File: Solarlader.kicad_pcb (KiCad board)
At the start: 2 copper layers, 32.8 x 29 mm, 40 parts, among them J3 UKDBBTAAA, Q1 HJ8205, Q2 AO3400A, U1 LGS5600, U2 DW01A, U3 74AHC1G14GV,125

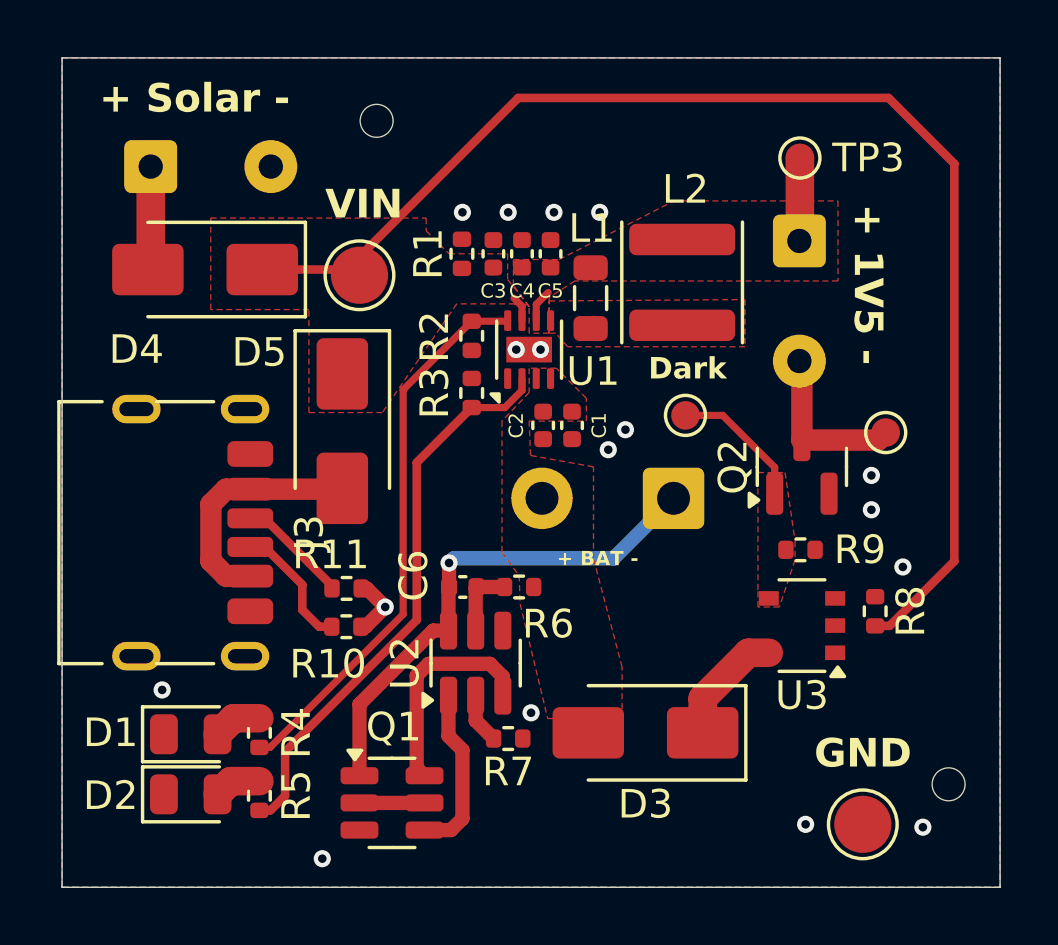
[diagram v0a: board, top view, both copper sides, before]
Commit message: Stand mit 1.5V
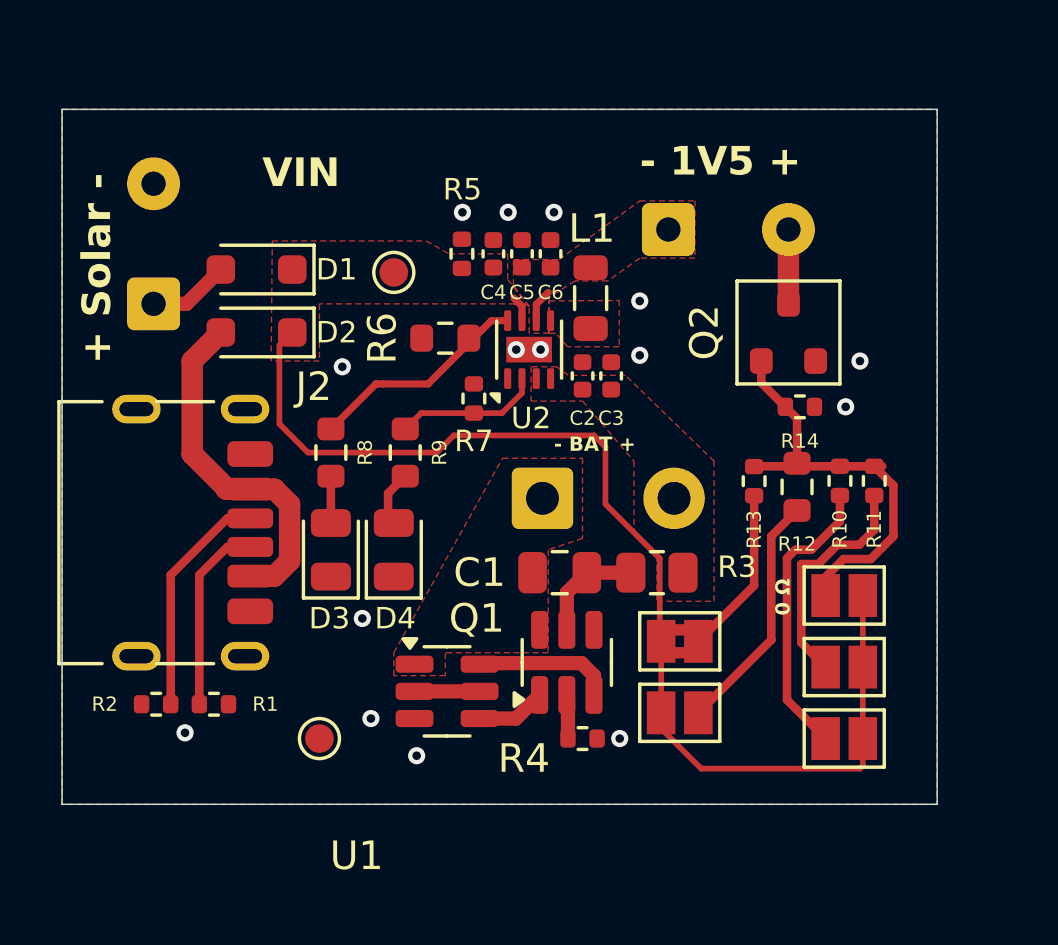
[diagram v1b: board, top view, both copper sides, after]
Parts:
- removed the D3 at (156.4, 95.4)
- removed L2: 2.2u, Inductor_SMD:L_APV_ANR4010
- removed the R8 at (164.4, 91.2)
- removed the R9 at (161.8, 89.0)
- removed REF** (x2): ToolingHole_1.152mm, MountingHole:ToolingHole_1.152mm
- removed TP3: +1V5, TestPoint:TestPoint_Pad_D1.0mm
- removed TP5: Switch+, TestPoint:TestPoint_Pad_D1.0mm
- removed TP6: Dark, TestPoint:TestPoint_Pad_D1.0mm
- removed U3: 74AHC1G14GV,125, Package_SO:TSOP-5_1.65x3.05mm_P0.95mm
- added JP1: SolderJumper_2_Open, Jumper:SolderJumper-2_P1.3mm_Open_Pad1.0x1.5mm, F.Cu at (163.3, 90.6)
- added JP2: SolderJumper_2_Open, Jumper:SolderJumper-2_P1.3mm_Open_Pad1.0x1.5mm, F.Cu at (163.3, 95.6)
- added JP3: SolderJumper_2_Open, Jumper:SolderJumper-2_P1.3mm_Open_Pad1.0x1.5mm, F.Cu at (163.3, 93.1)
- added JP4: SolderJumper_2_Open, Jumper:SolderJumper-2_P1.3mm_Open_Pad1.0x1.5mm, F.Cu at (157.6, 94.7)
- added JP5: SolderJumper_2_Bridged, Jumper:SolderJumper-2_P1.3mm_Bridged2Bar_Pad1.0x1.5mm, F.Cu at (157.6, 92.2)
- added R10: 2.2k, Resistor_SMD:R_0402_1005Metric, F.Cu at (163.2, 86.6)
- added R11: 5.1k, Resistor_SMD:R_0402_1005Metric, F.Cu at (164.4, 86.6)
- added R12: 8.2k, Resistor_SMD:R_0603_1608Metric, F.Cu at (161.7, 86.8)
- added R13: 10k, Resistor_SMD:R_0402_1005Metric, F.Cu at (160.2, 86.6)
- added R14: 100k, Resistor_SMD:R_0402_1005Metric, F.Cu at (161.8, 84.0)
- C1: renamed from C6; footprint Capacitor_SMD:C_0402_1005Metric -> Capacitor_SMD:C_0805_2012Metric
- D1: renamed from D4; value MDD SS14 -> 1N5819WS; footprint Diode_SMD:D_SMA -> Diode_SMD:D_SOD-323_HandSoldering
- D2: renamed from D5; value MDD SS14 -> 1N5819WS; footprint Diode_SMD:D_SMA -> Diode_SMD:D_SOD-323_HandSoldering
- Q2: footprint Package_TO_SOT_SMD:SOT-23 -> PCM_Package_TO_SOT_SMD_AKL:SOT-23
- R3: renamed from R6; footprint Resistor_SMD:R_0402_1005Metric -> Resistor_SMD:R_0805_2012Metric
- R6: renamed from R2; value 27k -> 30k; footprint Resistor_SMD:R_0402_1005Metric -> Resistor_SMD:R_0603_1608Metric
- R8: renamed from R4; value 150 -> 1.5k; footprint Resistor_SMD:R_0402_1005Metric -> Resistor_SMD:R_0603_1608Metric
- R9: renamed from R5; value 75 -> 1k; footprint Resistor_SMD:R_0402_1005Metric -> Resistor_SMD:R_0603_1608Metric
- TP1: renamed from TP2; footprint TestPoint:TestPoint_Pad_D2.0mm -> TestPoint:TestPoint_Pad_D1.0mm
- TP2: renamed from TP7; value Switch- -> GND; footprint TestPoint:TestPoint_Pad_D2.0mm -> TestPoint:TestPoint_Pad_D1.0mm
- moved TP2 19.2 mm to (145.0, 95.6)
- moved R9 13.0 mm to (148.0, 85.6), turned to -90 degrees
- moved D4 11.1 mm to (147.6, 89.0), turned to 90 degrees
- moved R8 10.1 mm to (145.4, 85.6), turned to -90 degrees
- moved D3 8.10 mm to (145.4, 89.0), turned to 90 degrees
- moved R2 7.79 mm to (139.3, 94.4), turned to 180 degrees
- moved R1 5.36 mm to (141.3, 94.4)
- moved R3 4.84 mm to (156.8, 89.8)
- moved J1 4.80 mm to (139.2, 80.4), turned to 90 degrees
- moved Q2 4.72 mm to (161.4, 81.4)
- moved J3 4.60 mm to (157.2, 77.8), turned to 0 degrees
- moved BT1 4.58 mm to (152.8, 87.2), turned to 0 degrees
- moved D2 4.57 mm to (142.8, 81.4), turned to 180 degrees
- moved Q1 4.35 mm to (149.5, 94.0)
- moved C1 3.42 mm to (153.4, 89.8)
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- renumbered C1 to C2, C2 to C3, C3 to C4, C4 to C5, C5 to C6, D1 to D3, D2 to D4, J2 to J1, J3 to J2, J1 to J3, R10 to R1, R11 to R2, R7 to R4, R1 to R5, R3 to R7, U2 to U1, U1 to U2
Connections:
- net /Switch+ renamed /Load+
- Q2 pad 1: /Dark -> Net-(JP1-A)
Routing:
- net /BAT-: track 18.5 -> 0.00 mm, vias 1 -> 0
- net Net-(JP1-A): track 0.00 -> 15.1 mm
- net Net-(U2-VSET/LED1): track 19.8 -> 5.11 mm
- net Net-(U2-ISET/LED2): track 19.5 -> 8.00 mm
- net Net-(JP2-A): track 0.00 -> 10.2 mm
- net Net-(JP4-A): track 0.00 -> 8.50 mm
- net Net-(JP3-A): track 0.00 -> 8.20 mm
- net Net-(JP5-A): track 0.00 -> 5.90 mm
- net Vin: track 46.2 -> 40.8 mm
- net /VBUS: track 8.40 -> 13.2 mm
- net /Dark: track 4.79 -> 0.00 mm
- net Net-(J2-CC1): track 4.16 -> 8.72 mm
- net Net-(D3-K): track 4.17 -> 0.00 mm
- net Net-(Q1-G1): track 5.99 -> 2.44 mm
- net /Load+: track 5.98 -> 2.60 mm
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- added copper zone on F.Cu, net /BAT-
- removed copper zone on F.Cu, net /Dark
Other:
- board size 32.8 x 29 mm -> 30.6 x 24.3 mm
- board text added: "- 1V5 +"
- board text added: "- BAT +"
- board text added: "0 Ω"
- board text removed: "+ 1V5 -"
- board text removed: "+ BAT -"
- board text removed: "Dark"
- board text removed: "GND"

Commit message: V2
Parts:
- removed JP1, JP2, JP3, JP4: SolderJumper_2_Open, Jumper:SolderJumper-2_P1.3mm_Open_Pad1.0x1.5mm
- removed JP5: SolderJumper_2_Bridged, Jumper:SolderJumper-2_P1.3mm_Bridged2Bar_Pad1.0x1.5mm
- removed Q2: AO3400A, PCM_Package_TO_SOT_SMD_AKL:SOT-23
- removed TP2: GND, TestPoint:TestPoint_Pad_D1.0mm
- added C10: 100u, Capacitor_Tantalum_SMD:CP_EIA-3528-21_Kemet-B, F.Cu at (178.5, 119.0)
- added C7: 10u, Capacitor_SMD:C_0603_1608Metric, F.Cu at (149.3, 107.0)
- added C8: 10u, Capacitor_SMD:C_0402_1005Metric, F.Cu at (152.9, 122.9)
- added C9: 20u, Capacitor_SMD:C_1206_3216Metric, F.Cu at (181.0, 129.5)
- added D5: KT-0805G, LED_SMD:LED_0805_2012Metric, F.Cu at (170.7, 105.2)
- added L2: 2.2u, Inductor_SMD:L_APV_ANR4020, F.Cu at (158.2, 124.8)
- added R15: 100k, Resistor_SMD:R_0402_1005Metric, F.Cu at (173.7, 124.8)
- added R16: 100, Resistor_SMD:R_0402_1005Metric, F.Cu at (173.7, 126.8)
- added R17: 100k, Resistor_SMD:R_0402_1005Metric, F.Cu at (173.7, 128.8)
- added R18: 0, Resistor_SMD:R_0603_1608Metric, F.Cu at (153.3, 109.5)
- added R19: 0, Resistor_SMD:R_0603_1608Metric, F.Cu at (153.3, 112.0)
- added U3: DW01A, Package_TO_SOT_SMD:SOT-23-6, F.Cu at (171.9, 113.8)
- added U4: TPS61022, Package_DFN_QFN:Texas_RWU0007A_VQFN-7_2x2mm_P0.5mm, F.Cu at (149.5, 125.2)
- BT1: footprint Connector_Wire:SolderWire-0.5sqmm_1x02_P4.6mm_D0.9mm_OD2.1mm -> Connector_JST:JST_PH_S2B-PH-K_1x02_P2.00mm_Horizontal
- C1: value 100n -> 100u; footprint Capacitor_SMD:C_0805_2012Metric -> Capacitor_Tantalum_SMD:CP_EIA-3528-21_Kemet-B
- C2, C4: footprint Capacitor_SMD:C_0402_1005Metric -> Capacitor_SMD:C_0603_1608Metric
- C3: value 10u -> 20u; footprint Capacitor_SMD:C_0402_1005Metric -> Capacitor_SMD:C_1206_3216Metric
- C5: value 10u -> 1u
- C6: value 10u -> 100n; footprint Capacitor_SMD:C_0402_1005Metric -> Capacitor_SMD:C_0805_2012Metric
- D1, D2: value 1N5819WS -> DSL34; footprint Diode_SMD:D_SOD-323_HandSoldering -> Diode_SMD:D_SOD-123F
- D3: value KT-0805Y -> DSL34; footprint LED_SMD:LED_0805_2012Metric -> Diode_SMD:D_SOD-123F
- D4: value KT-0805G -> KT-0805Y
- J1, J3: footprint Connector_Wire:SolderWire-0.25sqmm_1x02_P4.2mm_D0.65mm_OD1.7mm -> Connector_Wire:SolderWire-0.1sqmm_1x02_P3.6mm_D0.4mm_OD1mm
- L1: footprint Inductor_SMD:L_0805_2012Metric -> Inductor_SMD:L_APV_ANR4020
- R10: value 2.2k -> 1.6k; footprint Resistor_SMD:R_0402_1005Metric -> Resistor_SMD:R_0603_1608Metric
- R11: value 5.1k -> 1k
- R12: value 8.2k -> 51k; footprint Resistor_SMD:R_0603_1608Metric -> Resistor_SMD:R_0402_1005Metric
- R13: value 10k -> 680k; footprint Resistor_SMD:R_0402_1005Metric -> Resistor_SMD:R_0603_1608Metric
- R14: value 100k -> 2k
- R3: value 100 -> 51k; footprint Resistor_SMD:R_0805_2012Metric -> Resistor_SMD:R_0402_1005Metric
- R4: value 1k -> 680k; footprint Resistor_SMD:R_0402_1005Metric -> Resistor_SMD:R_0603_1608Metric
- R5: value 1k -> 2k
- R6: value 30k -> 100k; footprint Resistor_SMD:R_0603_1608Metric -> Resistor_SMD:R_0402_1005Metric
- R7: value 10k -> 1k; footprint Resistor_SMD:R_0402_1005Metric -> Resistor_SMD:R_0603_1608Metric
- R8: value 1.5k -> 1k
- R9: value 1k -> 100; footprint Resistor_SMD:R_0603_1608Metric -> Resistor_SMD:R_0805_2012Metric
- TP1: value VIn -> GND
- U1: value DW01A -> TPS61022; footprint Package_TO_SOT_SMD:SOT-23-6 -> Package_DFN_QFN:Texas_RWU0007A_VQFN-7_2x2mm_P0.5mm
- U2: value LGS5600 -> TP4056; footprint Package_DFN_QFN:DFN-8-1EP_2x2mm_P0.5mm_EP0.9x1.6mm -> Package_SO:SOP-8-1EP_4.57x4.57mm_P1.27mm_EP4.57x4.45mm
- moved J2 75.0 mm to (210.1, 113.3), turned to 90 degrees
- moved R2 72.3 mm to (206.7, 120.6), turned to -90 degrees
- moved R1 71.3 mm to (207.6, 120.6), turned to -90 degrees
- moved J1 68.9 mm to (201.8, 109.2), turned to 180 degrees
- moved D2 67.9 mm to (203.2, 112.2), turned to 0 degrees
- moved U2 65.3 mm to (198.6, 128.1), turned to 0 degrees
- moved D1 65.0 mm to (198.8, 112.2)
- moved C1 56.5 mm to (203.5, 116.0), turned to -90 degrees
- moved C2 56.2 mm to (198.8, 117.2), turned to -90 degrees
- moved C3 52.4 mm to (193.5, 118.7)
- moved R5 51.3 mm to (167.9, 126.8), turned to 0 degrees
- moved R6 50.7 mm to (167.9, 128.8), turned to 0 degrees
- moved C6 50.4 mm to (163.2, 128.0), turned to 0 degrees
- moved U1 49.9 mm to (196.5, 118.5), turned to 0 degrees
- moved TP1 46.4 mm to (153.0, 125.4)
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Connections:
- BT1 pad 1: /BAT- -> +BATT
- BT1 pad 2: /BAT+ -> /BAT-
- C1 pad 1: Net-(U1-VCC) -> /VIN
- C1 pad 2: /BAT- -> GND
- C2 pad 1: /BAT+ -> /VIN
- C3 pad 1: /BAT+ -> +5V
- C4 pad 1: Vin -> +5V
- C5 pad 1: +1V5 -> +5V
- C6 pad 1: +1V5 -> Net-(U3-VCC)
- C6 pad 2: GND -> /BAT-
- D1 pad 1: Vin -> /VIN
- D2 pad 1: Vin -> /VIN
- D3 pad 1: GND -> +5V
- D3 pad 2: Net-(D3-A) -> /VIN
- D4 pad 1: GND -> Net-(D4-K)
- D4 pad 2: Net-(D4-A) -> +5V
- J3 pad 1: +1V5 -> /VIN
- L1 pad 1: Net-(U2-LX) -> /VIN
- L1 pad 2: +1V5 -> Net-(U1-SW)
- R10 pad 1: Net-(JP2-A) -> Net-(U2-PROG)
- R10 pad 2: Net-(JP1-A) -> GND
- R11 pad 1: Net-(JP3-A) -> GND
- R11 pad 2: Net-(JP1-A) -> Net-(U3-CS)
- R12 pad 1: Net-(JP4-A) -> +4V5
- R12 pad 2: Net-(JP1-A) -> Net-(R12-Pad2)
- R13 pad 1: Net-(JP5-A) -> Net-(R12-Pad2)
- R13 pad 2: Net-(JP1-A) -> Net-(R13-Pad2)
- R14 pad 1: Net-(JP1-A) -> Net-(R13-Pad2)
- R14 pad 2: GND -> Net-(U4-FB)
- R3 pad 1: /BAT+ -> +5V
- R3 pad 2: Net-(U1-VCC) -> Net-(R3-Pad2)
- R4 pad 1: GND -> Net-(R3-Pad2)
- R4 pad 2: Net-(U1-CS) -> Net-(R4-Pad2)
- R5 pad 1: Vin -> Net-(R4-Pad2)
- R5 pad 2: GND -> Net-(U1-FB)
- R6 pad 1: Net-(U2-ISET/LED2) -> Net-(U1-FB)
- R7 pad 1: GND -> Net-(D4-K)
- R7 pad 2: Net-(U2-VSET/LED1) -> Net-(U2-STDBY)
- R8 pad 1: Net-(U2-ISET/LED2) -> Net-(D5-K)
- R8 pad 2: Net-(D3-A) -> Net-(U2-~{CHRG})
- R9 pad 1: Net-(U2-VSET/LED1) -> +BATT
- R9 pad 2: Net-(D4-A) -> Net-(U3-VCC)
- TP1 pad 1: Vin -> GND
- U1 pad 1: Net-(Q1-G1) -> GND
- U1 pad 2: Net-(U1-CS) -> Net-(U1-SW)
- U1 pad 3: Net-(Q1-G2) -> +5V
- U1 pad 4: unconnected-(U1-TD-Pad4) -> Net-(U1-FB)
- U1 pad 5: Net-(U1-VCC) -> /VIN
- U1 pad 6: /BAT- -> GND
- U2 pad 1: GND -> Net-(U2-~{CHRG})
- U2 pad 2: Net-(U2-VSET/LED1) -> GND
- U2 pad 3: /BAT+ -> +BATT
- U2 pad 4: /BAT+ -> +5V
- U2 pad 5: Net-(U2-LX) -> Net-(U2-STDBY)
- U2 pad 6: +1V5 -> Net-(U2-PROG)
- U2 pad 7: Vin -> (no net)
- U2 pad 8: Net-(U2-ISET/LED2) -> (no net)
- U2 pad 9: GND -> (no net)
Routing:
- net Vin: track 40.8 -> 0.00 mm
- net Net-(JP1-A): track 15.1 -> 0.00 mm
- net /VBUS: track 13.2 -> 0.00 mm
- net Net-(JP2-A): track 10.2 -> 0.00 mm
- net Net-(JP4-A): track 8.50 -> 0.00 mm
- net Net-(JP3-A): track 8.20 -> 0.00 mm
- net Net-(U2-ISET/LED2): track 8.00 -> 0.00 mm
- net Net-(JP5-A): track 5.90 -> 0.00 mm
- net Net-(U2-VSET/LED1): track 5.11 -> 0.00 mm
- net Net-(Q1-G2): track 4.87 -> 0.00 mm
- net GND: track 0.23 -> 4.99 mm, vias 15 -> 0
- net Net-(U1-VCC): track 3.83 -> 0.00 mm
- net /Solar+: track 3.45 -> 0.00 mm
- net Net-(J2-CC2): track 7.31 -> 10.4 mm
- net /Load+: track 2.60 -> 0.00 mm
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- added copper zone on In1.Cu, net GND
- added copper zone on In2.Cu, net GND
- removed copper zone on F.Cu, net +1V5
- removed copper zone on F.Cu, net /BAT+
- removed copper zone on F.Cu, net /BAT-
- removed copper zone on F.Cu, net GND
- removed copper zone on F.Cu, net Net-(U2-LX)
- removed copper zone on F.Cu, net Vin
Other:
- board size 30.6 x 24.3 mm -> 29 x 31.8 mm
- copper layers 2 -> 4
- rule pad_to_mask_clearance: 0 -> 0.038
- board text added: "- IN +"
- board text added: "USB 5V"
- board text removed: "+ Solar -"
- board text removed: "- 1V5 +"
- board text removed: "- BAT +"
- board text removed: "0 Ω"
- board text removed: "VIN"

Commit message: Saved between
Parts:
- removed C7: 10u, Capacitor_SMD:C_0603_1608Metric
- removed C8: 10u, Capacitor_SMD:C_0402_1005Metric
- removed C9: 20u, Capacitor_SMD:C_1206_3216Metric
- removed D5: KT-0805G, LED_SMD:LED_0805_2012Metric
- removed J3: ~, Connector_Wire:SolderWire-0.1sqmm_1x02_P3.6mm_D0.4mm_OD1mm
- removed L1, L2: 2.2u, Inductor_SMD:L_APV_ANR4020
- removed R10: 1.6k, Resistor_SMD:R_0603_1608Metric
- removed R12: 51k, Resistor_SMD:R_0402_1005Metric
- removed R13: 680k, Resistor_SMD:R_0603_1608Metric
- removed R14: 2k, Resistor_SMD:R_0402_1005Metric
- removed R15, R17: 100k, Resistor_SMD:R_0402_1005Metric
- removed R16: 100, Resistor_SMD:R_0402_1005Metric
- removed R18, R19: 0, Resistor_SMD:R_0603_1608Metric
- removed R8: 1k, Resistor_SMD:R_0603_1608Metric
- removed TP1: GND, TestPoint:TestPoint_Pad_D1.0mm
- removed U2: TP4056, Package_SO:SOP-8-1EP_4.57x4.57mm_P1.27mm_EP4.57x4.45mm
- removed U4: TPS61022, Package_DFN_QFN:Texas_RWU0007A_VQFN-7_2x2mm_P0.5mm
- added H1: MountingHole, MountingHole:MountingHole_2.2mm_M2_DIN965, F.Cu at (188.0, 108.4)
- added H2: MountingHole, MountingHole:MountingHole_2.2mm_M2_DIN965, F.Cu at (211.5, 127.1)
- C2: value 10u -> 2.2u 25V; footprint Capacitor_SMD:C_0603_1608Metric -> Capacitor_SMD:C_0805_2012Metric
- C3: value 20u -> 0.1u 25V; footprint Capacitor_SMD:C_1206_3216Metric -> Capacitor_SMD:C_0402_1005Metric
- C4: value 10u -> 1u 35V
- C5: value 1u -> 10p 10V
- D3: value DSL34 -> KT-0603W; footprint Diode_SMD:D_SOD-123F -> LED_SMD:LED_0603_1608Metric
- D4: value KT-0805Y -> KT-0603Y2; footprint LED_SMD:LED_0805_2012Metric -> LED_SMD:LED_0603_1608Metric
- R3: value 51k -> 18k
- R4: value 680k -> 620
- R5: value 2k -> 10k
- R6: value 100k -> 510
- R7: value 1k -> 300; footprint Resistor_SMD:R_0603_1608Metric -> Resistor_SMD:R_0402_1005Metric
- U1: value TPS61022 -> BQ25185; footprint Package_DFN_QFN:Texas_RWU0007A_VQFN-7_2x2mm_P0.5mm -> Snapeda:WSON10_DLH_TEX-L
- U3: value DW01A -> DW01A - C686633
- moved R7 56.5 mm to (205.2, 120.1), turned to 90 degrees
- moved R4 55.4 mm to (204.1, 117.9)
- moved C4 55.2 mm to (201.6, 122.1)
- moved C5 46.0 mm to (198.9, 120.1), turned to 90 degrees
- moved D3 43.6 mm to (207.2, 120.6), turned to 180 degrees
- moved R9 42.0 mm to (199.1, 123.0), turned to -90 degrees
- moved D4 41.8 mm to (207.2, 122.2), turned to 180 degrees
- moved Q1 38.3 mm to (206.3, 125.9), turned to 90 degrees
- moved R6 37.8 mm to (205.2, 122.6), turned to -90 degrees
- moved BT1 36.7 mm to (192.0, 123.7), turned to -90 degrees
- moved C6 35.9 mm to (199.1, 126.4), turned to -90 degrees
- moved R5 35.9 mm to (203.2, 120.1)
- moved R3 35.7 mm to (203.2, 119.1)
- moved U3 32.6 mm to (202.1, 125.9), turned to 180 degrees
- moved R11 30.2 mm to (201.0, 123.7)
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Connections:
- net /BAT- renamed -BATT
- net Net-(U3-CS) renamed /CS
- net Net-(U3-VCC) renamed /VCC
- C1 pad 1: /VIN -> VIN
- C2 pad 1: /VIN -> VIN
- C3 pad 1: +5V -> VIN
- C4 pad 1: +5V -> +BATT
- C5 pad 1: +5V -> VSYS
- D1 pad 1: /VIN -> VIN
- D2 pad 1: /VIN -> VIN
- D3 pad 1: +5V -> /STAT1
- D3 pad 2: /VIN -> Net-(D3-A)
- D4 pad 1: Net-(D4-K) -> /STAT2
- D4 pad 2: +5V -> Net-(D4-A)
- R3 pad 1: +5V -> /ILIM
- R3 pad 2: Net-(R3-Pad2) -> GND
- R4 pad 1: Net-(R3-Pad2) -> /ISET
- R4 pad 2: Net-(R4-Pad2) -> GND
- R5 pad 1: Net-(R4-Pad2) -> /TS/MR
- R5 pad 2: Net-(U1-FB) -> GND
- R6 pad 1: Net-(U1-FB) -> VSYS
- R6 pad 2: GND -> Net-(D4-A)
- R7 pad 1: Net-(D4-K) -> VSYS
- R7 pad 2: Net-(U2-STDBY) -> Net-(D3-A)
- U1 pad 1: GND -> VSYS
- U1 pad 2: Net-(U1-SW) -> +BATT
- U1 pad 3: +5V -> /STAT2
- U1 pad 4: Net-(U1-FB) -> GND
- U1 pad 5: /VIN -> GND
- U1 pad 6: GND -> /TS/MR
- U1 pad 7: /VIN -> /ILIM
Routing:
- net Net-(Q1-D1/D2-Pad2): track 0.00 -> 9.36 mm, vias 0 -> 2
- net /VBUS: track 0.00 -> 6.49 mm
- net /Solar+: track 0.00 -> 5.84 mm
- net Net-(Q1-G1): track 0.00 -> 5.26 mm
- net GND: track 4.99 -> 0.00 mm, vias 0 -> 26
- net /ISET: track 0.00 -> 3.64 mm
- net /VCC: track 0.00 -> 3.62 mm
- net /CS: track 0.00 -> 3.32 mm
- net /ILIM: track 0.00 -> 3.31 mm
- net /TS/MR: track 0.00 -> 2.43 mm
- net Net-(Q1-G2): track 0.00 -> 2.19 mm
- net Net-(J2-CC2): track 10.4 -> 12.3 mm
- net Net-(D3-A): track 0.00 -> 1.61 mm
- net Net-(D4-A): track 0.00 -> 1.60 mm
- net Net-(J2-CC1): track 7.96 -> 9.26 mm
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- added copper zone on F.Cu, net +BATT
- added copper zone on F.Cu, net -BATT
- added copper zone on F.Cu, net GND
- added copper zone on F.Cu, net VIN
- added copper zone on B.Cu, net VSYS
- added copper zone on F.Cu, net VSYS
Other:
- board size 29 x 31.8 mm -> 29 x 24.4 mm
